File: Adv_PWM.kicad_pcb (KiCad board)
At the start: 2 copper layers, 37.2 x 29 mm, 13 parts, among them IC1 ATTINY13-P, P1 CONN_01X03, P2 CONN_01X03, SW1 Rotary_Encoder_Switch, U1 LTV-817

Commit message: INT0 changes
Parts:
- R3: footprint Resistors_THT:R_Axial_DIN0204_L3.6mm_D1.6mm_P5.08mm_Horizontal -> Resistors_THT:R_Axial_DIN0204_L3.6mm_D1.6mm_P7.62mm_Horizontal
- moved R3 2.16 mm to (147.3, 81.0)
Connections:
- IC1 pad 6: /PWM -> /IN
- IC1 pad 7: /IN -> /PWM
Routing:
- net /PWM: track 12.7 -> 9.41 mm
- net /IN: track 12.7 -> 15.2 mm
- net +5V: track 9.06 -> 9.75 mm

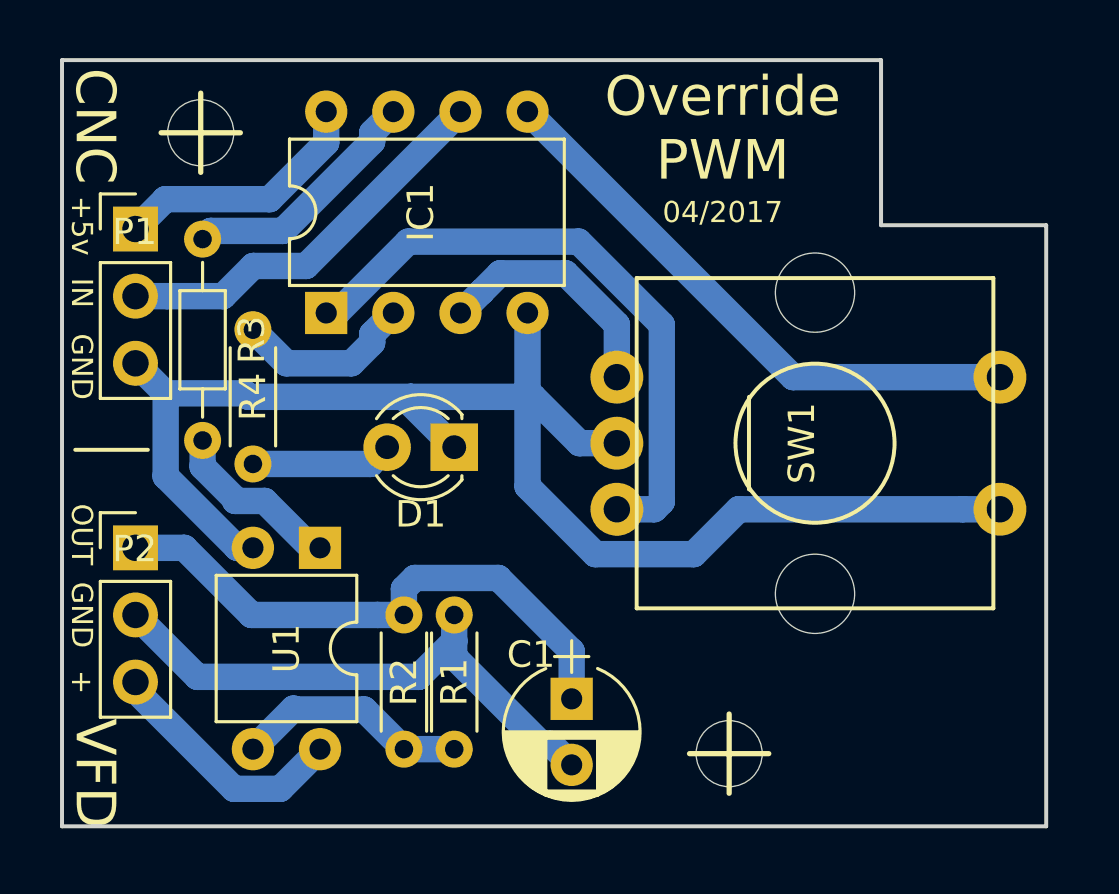
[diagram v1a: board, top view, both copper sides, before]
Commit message: Compactify a little more
This includes adding a single surface mount resistor!
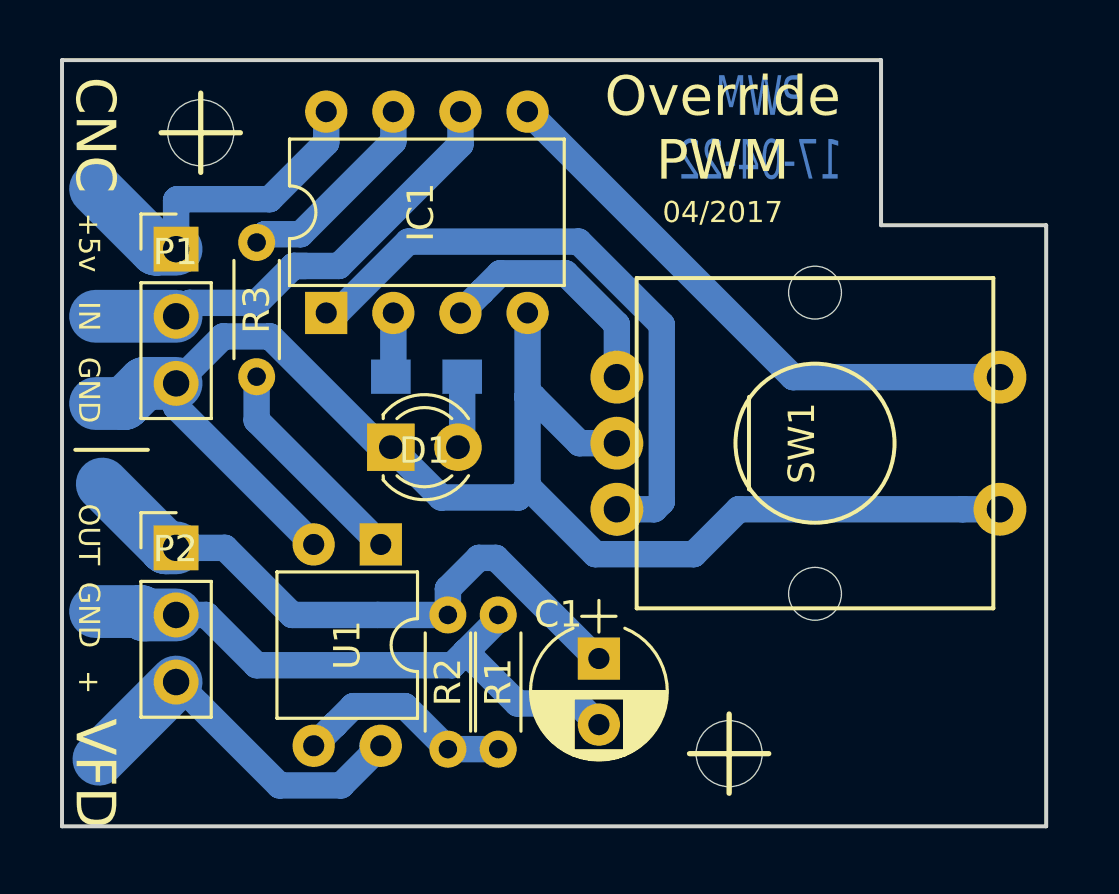
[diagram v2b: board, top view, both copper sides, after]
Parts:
- R3: footprint Resistors_THT:R_Axial_DIN0204_L3.6mm_D1.6mm_P7.62mm_Horizontal -> Resistors_THT:R_Axial_DIN0204_L3.6mm_D1.6mm_P5.08mm_Horizontal
- R4: footprint Resistors_THT:R_Axial_DIN0204_L3.6mm_D1.6mm_P5.08mm_Horizontal -> Resistors_SMD:R_0805_HandSoldering; moved to B.Cu
- moved R4 6.81 mm to (155.8, 86.2), turned to 0 degrees
- moved D1 2.40 mm to (154.4, 88.9), turned to 0 degrees
- moved U1 2.30 mm to (154.1, 92.6)
- moved R3 2.05 mm to (149.4, 81.2)
- moved C1 1.84 mm to (162.3, 96.9)
- moved P1 1.72 mm to (146.3, 81.4)
- moved R1 1.66 mm to (158.5, 95.2)
- moved R2 1.66 mm to (156.6, 95.2)
- moved P2 1.54 mm to (146.3, 92.7)
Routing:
- net VCC: track 9.46 -> 14.4 mm
- net Net-(IC1-Pad2): track 6.82 -> 2.45 mm
- net +5V: track 9.75 -> 13.6 mm
- net /IN: track 15.2 -> 18.2 mm
- net GND: track 56.2 -> 58.9 mm
- net Net-(D1-Pad2): track 5.34 -> 2.73 mm
- net /Vref: track 21.7 -> 23.9 mm
- net GNDA: track 21.3 -> 23.1 mm
- net Net-(R3-Pad2): track 6.75 -> 8.30 mm
- net /PWM: track 9.41 -> 8.02 mm
- net Net-(R1-Pad2): track 8.89 -> 8.28 mm
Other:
- board text added: "PWM 17-04-22"

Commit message: Switch the PWM output to a clock pin
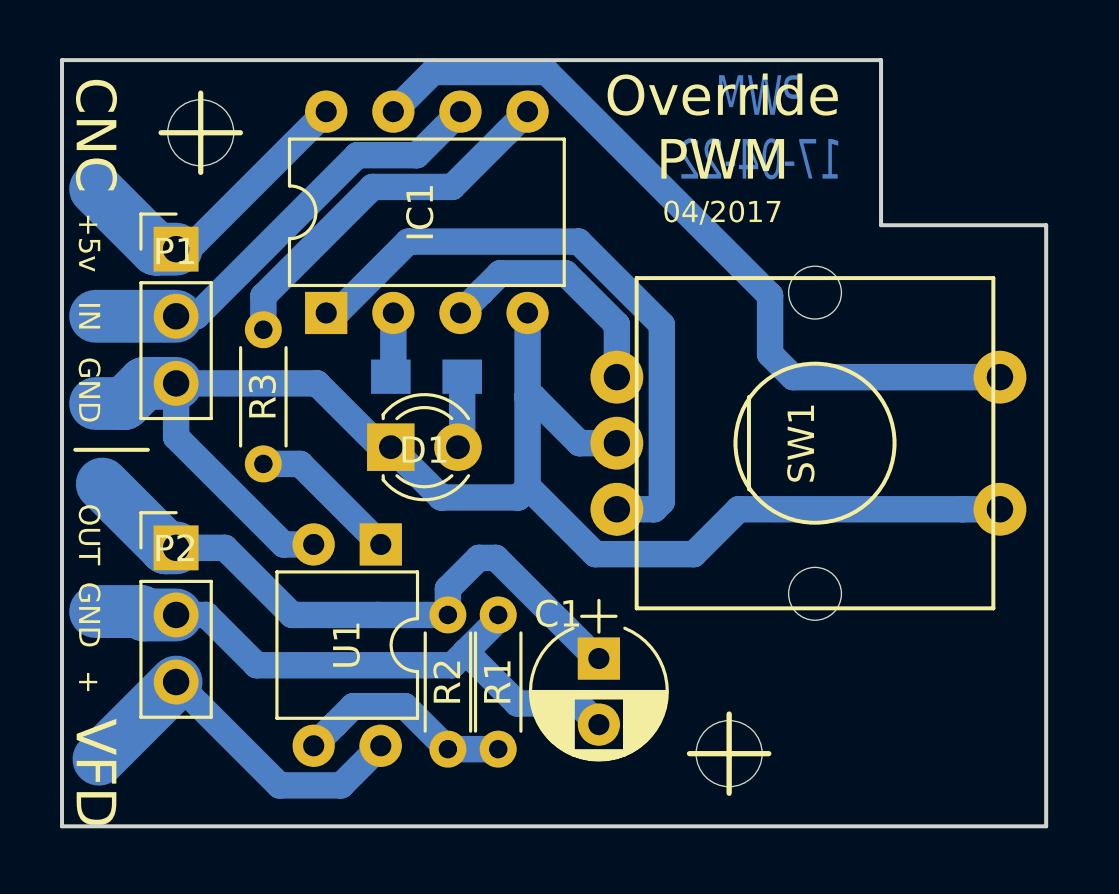
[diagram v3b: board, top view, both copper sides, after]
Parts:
- moved R3 3.31 mm to (149.6, 84.5)
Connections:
- IC1 pad 5: /SW -> /PWM
- IC1 pad 7: /PWM -> /SW
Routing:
- net /SW: track 22.0 -> 29.8 mm
- net /PWM: track 8.02 -> 14.2 mm
- net Net-(R3-Pad2): track 8.30 -> 5.71 mm
- net +5V: track 13.6 -> 11.8 mm
- net /IN: track 18.2 -> 17.0 mm
- net GND: track 58.9 -> 58.1 mm
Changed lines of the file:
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@@
   (general
     (links 21)
-    (no_connects 0)
+    (no_connects 2)
     (area 141.924999 74.174999 179.325001 103.325001)
     (thickness 1.6)
     (drawings 22)
-    (tracks 100)
+    (tracks 98)
     (zones 0)
     (modules 13)
@@
   )
   (setup
-    (last_trace_width 2)
+    (last_trace_width 1)
     (user_trace_width 0.2)
     (user_trace_width 0.3048)
@@
       (net 6 /B))
     (pad 5 thru_hole oval (at 7.62 7.62 90) (size 1.6 1.6) (drill 0.8) (layers *.Cu *.Mask)
-      (net 7 /SW))
+      (net 2 /PWM))
     (pad 2 thru_hole oval (at 0 2.54 90) (size 1.6 1.6) (drill 0.8) (layers *.Cu *.Mask)
       (net 14 "Net-(IC1-Pad2)"))
@@
       (net 8 /A))
     (pad 7 thru_hole oval (at 7.62 2.54 90) (size 1.6 1.6) (drill 0.8) (layers *.Cu *.Mask)
-      (net 2 /PWM))
+      (net 7 /SW))
     (pad 4 thru_hole oval (at 0 7.62 90) (size 1.6 1.6) (drill 0.8) (layers *.Cu *.Mask)
       (net 3 GND))
@@
   )
   (module Resistors_THT:R_Axial_DIN0204_L3.6mm_D1.6mm_P5.08mm_Horizontal (layer F.Cu)
-    (at 149.366 81.152 270)
+    (at 149.62 84.454 270)
     (descr "Resistor, Axial_DIN0204 series, Axial, Horizontal, pin pitch=5.08mm, 0.16666666666666666W = 1/6W, length*diameter=3.6*1.6mm^2, http://cdn-reichelt.de/documents/datenblatt/B400/1_4W%23YAG.pdf")
     (tags "Resistor Axial_DIN0204 series Axial Horizontal pin pitch 5.08mm 0.16666666666666666W = 1/6W length 3.6mm diameter 1.6mm")
@@
   (segment (start 158.51 95.417002) (end 157.281002 96.646) (width 1) (layer B.Cu) (net 1))
   (segment (start 158.51 95.25) (end 158.51 95.417002) (width 1) (layer B.Cu) (net 1))
-  (segment (start 149.366 81.152) (end 149.677009 80.840991) (width 1) (layer B.Cu) (net 2))
-  (segment (start 149.677009 80.840991) (end 151.030379 80.840991) (width 1) (layer B.Cu) (net 2))
-  (segment (start 151.030379 80.840991) (end 154.54 77.33137) (width 1) (layer B.Cu) (net 2))
-  (segment (start 154.54 77.33137) (end 154.54 76.2) (width 1) (layer B.Cu) (net 2))
-  (segment (start 154.446 76.294) (end 154.54 76.2) (width 1) (layer B.Cu) (net 2))
+  (segment (start 149.62 84.454) (end 149.62 83.184) (width 1) (layer B.Cu) (net 2))
+  (segment (start 149.62 83.184) (end 153.753989 79.050011) (width 1) (layer B.Cu) (net 2))
+  (segment (start 153.753989 79.050011) (end 156.769989 79.050011) (width 1) (layer B.Cu) (net 2))
+  (segment (start 156.769989 79.050011) (end 158.820001 76.999999) (width 1) (layer B.Cu) (net 2))
+  (segment (start 158.820001 76.999999) (end 159.62 76.2) (width 1) (layer B.Cu) (net 2))
+  (segment (start 151.525 92.582) (end 150.382 92.582) (width 1) (layer B.Cu) (net 3))
+  (segment (start 150.382 92.582) (end 146.318 88.518) (width 1) (layer B.Cu) (net 3))
+  (segment (start 146.318 88.518) (end 146.318 86.486) (width 1) (layer B.Cu) (net 3))
+  (segment (start 146.318 86.486) (end 151.652 86.486) (width 1) (layer B.Cu) (net 3))
+  (segment (start 151.652 86.486) (end 154.066 88.9) (width 1) (layer B.Cu) (net 3))
+  (segment (start 154.066 88.9) (end 154.446 88.9) (width 1) (layer B.Cu) (net 3))
   (segment (start 146.318 86.486) (end 145.115919 86.486) (width 2) (layer B.Cu) (net 3))
   (segment (start 145.115919 86.486) (end 144.353919 87.248) (width 2) (layer B.Cu) (net 3))
   (segment (start 144.353919 87.248) (end 143.27 87.248) (width 2) (layer B.Cu) (net 3))
-  (segment (start 146.318 86.486) (end 148.096 84.708) (width 1) (layer B.Cu) (net 3))
-  (segment (start 148.096 84.708) (end 149.874 84.708) (width 1) (layer B.Cu) (net 3))
-  (segment (start 149.874 84.708) (end 154.066 88.9) (width 1) (layer B.Cu) (net 3))
-  (segment (start 154.066 88.9) (end 154.446 88.9) (width 1) (layer B.Cu) (net 3))
-  (segment (start 151.525 92.582) (end 146.318 87.375) (width 1) (layer B.Cu) (net 3))
-  (segment (start 146.318 87.375) (end 146.318 86.486) (width 1) (layer B.Cu) (net 3))
   (segment (start 159.62 90.386002) (end 159.62 90.456) (width 1) (layer B.Cu) (net 3))
   (segment (start 159.62 90.456) (end 159.272 90.804) (width 1) (layer B.Cu) (net 3))
@@
   (segment (start 159.830787 86.995) (end 159.62 86.995) (width 1) (layer B.Cu) (net 3))
   (segment (start 161.585787 88.75) (end 159.830787 86.995) (width 1) (layer B.Cu) (net 3))
+  (segment (start 152 76.2) (end 146.794 81.406) (width 1) (layer B.Cu) (net 4))
+  (segment (start 146.794 81.406) (end 146.318 81.406) (width 1) (layer B.Cu) (net 4))
   (segment (start 145.556 81.406) (end 143.27 79.12) (width 2) (layer B.Cu) (net 4))
   (segment (start 146.318 81.406) (end 145.556 81.406) (width 2) (layer B.Cu) (net 4))
-  (segment (start 149.860022 79.514978) (end 146.359022 79.514978) (width 1) (layer B.Cu) (net 4))
-  (segment (start 146.359022 79.514978) (end 146.318 79.556) (width 1) (layer B.Cu) (net 4))
-  (segment (start 146.318 79.556) (end 146.318 81.406) (width 1) (layer B.Cu) (net 4))
-  (segment (start 152 76.2) (end 152 77.375) (width 1) (layer B.Cu) (net 4))
-  (segment (start 152 77.375) (end 149.860022 79.514978) (width 1) (layer B.Cu) (net 4))
   (segment (start 158.51 100.33) (end 156.605 100.33) (width 1) (layer B.Cu) (net 5))
   (segment (start 156.605 100.33) (end 154.976999 98.701999) (width 1) (layer B.Cu) (net 5))
@@
   (segment (start 152.4 83.82) (end 152 83.82) (width 1) (layer B.Cu) (net 6))
   (segment (start 163 91.75) (end 163.016002 91.75) (width 1) (layer B.Cu) (net 6))
+  (segment (start 154.54 76.2) (end 156.040001 74.699999) (width 1) (layer B.Cu) (net 7))
+  (segment (start 156.040001 74.699999) (end 160.340001 74.699999) (width 1) (layer B.Cu) (net 7))
+  (segment (start 160.340001 74.699999) (end 168.799999 83.159997) (width 1) (layer B.Cu) (net 7))
+  (segment (start 168.799999 83.159997) (end 168.799999 85.379999) (width 1) (layer B.Cu) (net 7))
+  (segment (start 168.799999 85.379999) (end 169.67 86.25) (width 1) (layer B.Cu) (net 7))
+  (segment (start 154.446 76.294) (end 154.54 76.2) (width 1) (layer B.Cu) (net 7))
   (segment (start 177.5 86.25) (end 169.67 86.25) (width 1) (layer B.Cu) (net 7))
-  (segment (start 169.67 86.25) (end 159.62 76.2) (width 1) (layer B.Cu) (net 7))
   (segment (start 163 84.26) (end 161.059999 82.319999) (width 1) (layer B.Cu) (net 8))
   (segment (start 161.059999 82.319999) (end 158.580001 82.319999) (width 1) (layer B.Cu) (net 8))
@@
   (segment (start 157.879999 83.020001) (end 157.08 83.82) (width 1) (layer B.Cu) (net 8))
   (segment (start 163 86.25) (end 163 84.26) (width 1) (layer B.Cu) (net 8))
+  (segment (start 157.08 76.2) (end 155.43 77.85) (width 1) (layer B.Cu) (net 9))
+  (segment (start 153.176 77.85) (end 147.08 83.946) (width 1) (layer B.Cu) (net 9))
+  (segment (start 155.43 77.85) (end 153.176 77.85) (width 1) (layer B.Cu) (net 9))
+  (segment (start 147.08 83.946) (end 146.318 83.946) (width 1) (layer B.Cu) (net 9))
   (segment (start 146.318 83.946) (end 143.27 83.946) (width 2) (layer B.Cu) (net 9))
-  (segment (start 150.763 82.041) (end 152.48193 82.041) (width 1) (layer B.Cu) (net 9))
-  (segment (start 152.48193 82.041) (end 157.08 77.44293) (width 1) (layer B.Cu) (net 9))
-  (segment (start 157.08 77.44293) (end 157.08 77.33137) (width 1) (layer B.Cu) (net 9))
-  (segment (start 157.08 77.33137) (end 157.08 76.2) (width 1) (layer B.Cu) (net 9))
-  (segment (start 146.318 83.946) (end 146.826 83.438) (width 1) (layer B.Cu) (net 9))
-  (segment (start 146.826 83.438) (end 149.366 83.438) (width 1) (layer B.Cu) (net 9))
-  (segment (start 149.366 83.438) (end 150.763 82.041) (width 1) (layer B.Cu) (net 9))
-  (segment (start 150.763 82.041) (end 151.239 82.041) (width 1) (layer B.Cu) (net 9))
-  (segment (start 149.366 86.232) (end 149.366 87.883) (width 1) (layer B.Cu) (net 10))
-  (segment (start 149.366 87.883) (end 154.065 92.582) (width 1) (layer B.Cu) (net 10))
+  (segment (start 149.62 89.534) (end 151.017 89.534) (width 1) (layer B.Cu) (net 10))
+  (segment (start 151.017 89.534) (end 154.065 92.582) (width 1) (layer B.Cu) (net 10))
   (segment (start 145.938 92.71) (end 143.524 90.296) (width 2) (layer B.Cu) (net 11))
   (segment (start 146.318 92.71) (end 145.938 92.71) (width 2) (layer B.Cu) (net 11))

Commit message: Use Voltage Divider on reset pin
this means that we no longer need the reset fuse to be set, allowing
reprogramming when testing. This required the swapping of pins and a
slightly more complicated board.
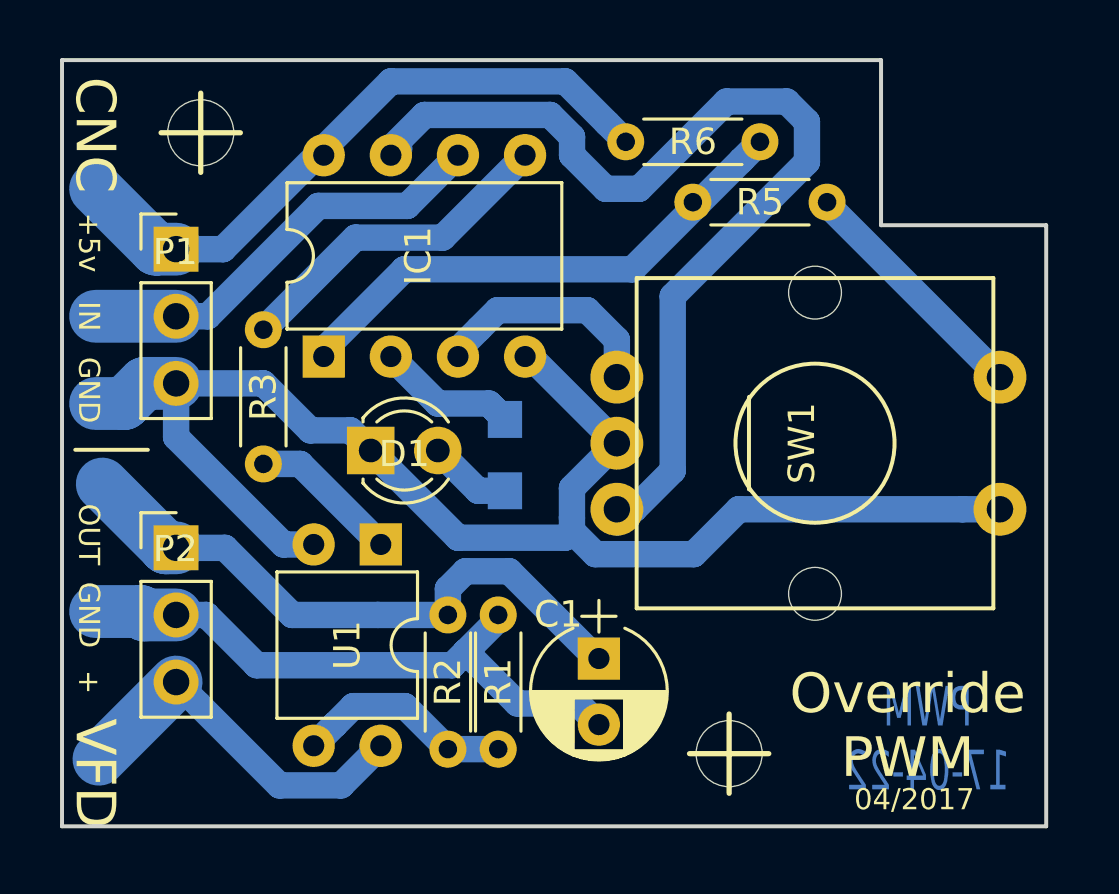
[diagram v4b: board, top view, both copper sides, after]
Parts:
- added R5: 33k, Resistors_THT:R_Axial_DIN0204_L3.6mm_D1.6mm_P5.08mm_Horizontal, F.Cu at (171.0, 79.6)
- added R6: 22k, Resistors_THT:R_Axial_DIN0204_L3.6mm_D1.6mm_P5.08mm_Horizontal, F.Cu at (168.4, 77.3)
- moved R4 4.20 mm to (158.8, 89.2), turned to 270 degrees
- moved IC1 1.65 mm to (151.9, 85.5)
- moved D1 0.77 mm to (153.7, 89.0)
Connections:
- IC1 pad 1: /B -> /SW
- IC1 pad 7: /SW -> /B
- SW1 pad 4: /SW -> Net-(R5-Pad1)
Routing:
- net /B: track 23.7 -> 37.9 mm
- net +5V: track 11.8 -> 25.1 mm
- net /SW: track 29.8 -> 19.8 mm
- net Net-(R5-Pad1): track 0.00 -> 9.33 mm
- net Net-(IC1-Pad2): track 2.45 -> 5.54 mm
- net GND: track 58.1 -> 56.1 mm
- net /PWM: track 14.2 -> 12.6 mm
- net /A: track 9.33 -> 8.51 mm

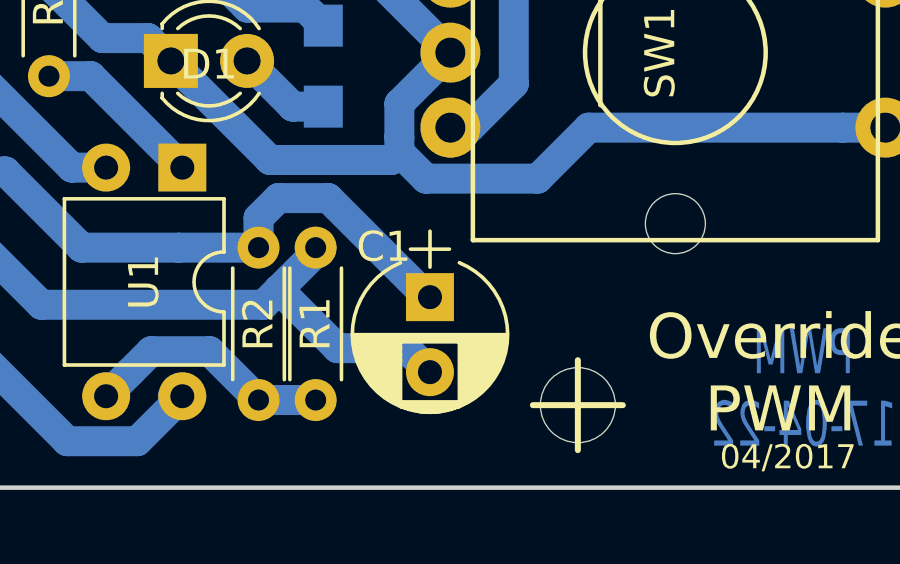
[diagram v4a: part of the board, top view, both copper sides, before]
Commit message: Change the capacitor footprint to be smaller
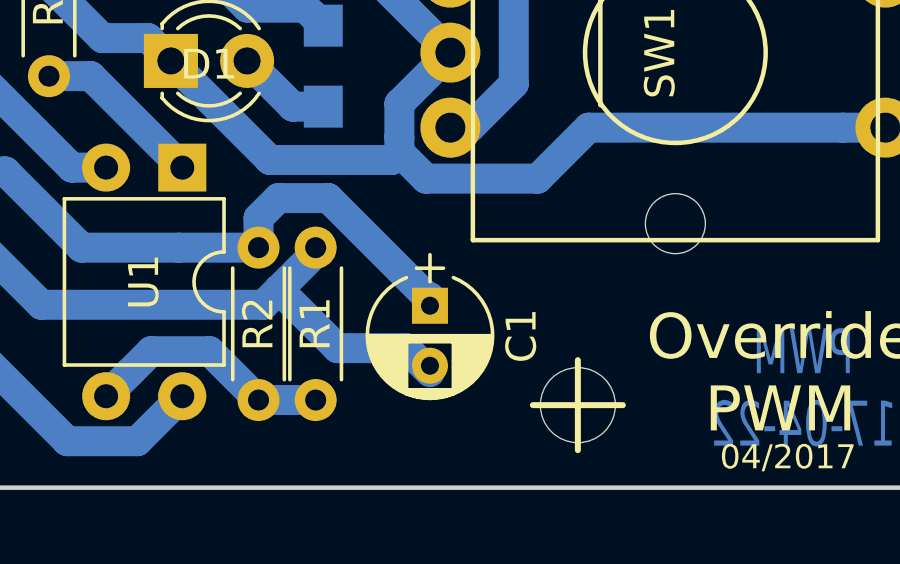
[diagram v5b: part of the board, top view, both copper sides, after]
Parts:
- C1: footprint Capacitors_THT:CP_Radial_D5.0mm_P2.50mm -> Capacitors_THT:CP_Radial_D4.0mm_P2.00mm
- moved C1 0.29 mm to (162.3, 97.2)
